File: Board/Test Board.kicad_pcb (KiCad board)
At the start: 2 copper layers, 165.1 x 76.2 mm, 29 parts, among them J1 SCREW TERMINAL, J2 SCREW TERMINAL, J3 SCREW TERMINAL, K1 FINDER-32.21-x300, K2 FINDER-32.21-x300, K3 FINDER-32.21-x300, SW1 UP-MJTP1230, SW2 LT-MJTP1230, SW3 DN-MJTP1230, SW4 RT-MJTP1230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

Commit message: Started re-engineering board
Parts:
- removed K1, K2, K3: FINDER-32.21-x300, Relay_THT:Relay_SPST_Finder_32.21-x300
- added U3: DS1E-M-DC5V, Arduino-Thermostat:DS1E-M-DC5V, F.Cu at (175.0, 34.4)
- added U4: DS1E-M-DC5V, Arduino-Thermostat:DS1E-M-DC5V, F.Cu at (86.2, 86.1)
- added U5: DS1E-M-DC5V, Arduino-Thermostat:DS1E-M-DC5V, F.Cu at (74.1, 86.1)
- C1, C2: value 680uF -> 220uF; footprint Capacitor_THT:CP_Radial_D12.5mm_P5.00mm -> Capacitor_THT:CP_Radial_D10.0mm_P5.00mm
- D2: value SB5199TA -> 31DQ05TA; footprint Diode_THT:D_DO-201_P15.24mm_Horizontal -> Diode_THT:D_DO-201AD_P5.08mm_Vertical_AnodeUp
- L1: footprint Inductor_THT:L_Toroid_Vertical_L21.6mm_W11.4mm_P7.62mm_Pulse_KM-3 -> Inductor_THT:L_Radial_D12.0mm_P5.00mm_Fastron_11P
- R1: value 220R -> XXR; footprint Resistor_THT:R_Axial_DIN0207_L6.3mm_D2.5mm_P7.62mm_Horizontal -> Resistor_SMD:R_1206_3216Metric
- R18, R19, R20, R21, R22: footprint Resistor_THT:R_Axial_DIN0207_L6.3mm_D2.5mm_P7.62mm_Horizontal -> Resistor_SMD:R_1206_3216Metric
- R23: value 220R -> 600R; footprint Resistor_THT:R_Axial_DIN0207_L6.3mm_D2.5mm_P7.62mm_Horizontal -> Resistor_SMD:R_1206_3216Metric
- U6: footprint Sensor:Aosong_DHT11_5.5x12.0_P2.54mm -> Arduino-Thermostat:DHT22-Horizontal
- moved J2 134.5 mm to (175.9, 55.3), turned to 0 degrees
- moved U6 125.0 mm to (75.2, 73.5), turned to 0 degrees
- moved RV1 101.5 mm to (102.4, 87.1), turned to 0 degrees
- moved U1 98.0 mm to (174.8, 69.9)
- moved R23 95.4 mm to (187.4, 40.7), turned to 0 degrees
- moved A1 94.6 mm to (155.1, 37.1), turned to 0 degrees
- moved R22 91.9 mm to (98.6, 99.5)
- moved J3 91.2 mm to (132.4, 88.4), turned to 0 degrees
- moved J1 88.2 mm to (132.4, 76.6), turned to 0 degrees
- moved R19 73.6 mm to (187.3, 34.1), turned to 0 degrees
- moved R18 64.2 mm to (187.3, 37.4)
- moved R21 60.4 mm to (123.6, 72.0)
- moved C1 60.3 mm to (118.8, 96.1), turned to 0 degrees
- moved D2 52.8 mm to (144.4, 85.3), turned to 0 degrees
- moved D1 50.7 mm to (106.9, 73.6), turned to 0 degrees
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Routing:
- net /DHT: track 106.0 -> 0.00 mm
- net Net-(DS1-Pad3): track 74.2 -> 0.00 mm
- net /R: track 67.2 -> 0.00 mm
- net /SW_RT: track 65.1 -> 0.00 mm
- net /COOL: track 63.9 -> 0.00 mm, vias 1 -> 0
- net /SW_UP: track 61.5 -> 0.00 mm
- net Net-(DS1-Pad15): track 60.9 -> 0.00 mm, vias 1 -> 0
- net /D7: track 54.6 -> 0.00 mm
- net /D4: track 54.6 -> 0.00 mm
- net /D6: track 54.6 -> 0.00 mm
- net /D5: track 54.6 -> 0.00 mm
- net /BKLT: track 54.0 -> 0.00 mm
- net +5V: track 52.9 -> 0.00 mm
- net /SW_DN: track 51.0 -> 0.00 mm
- net /E: track 44.1 -> 0.00 mm
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- removed copper zone on B.Cu, net +5V
- removed copper zone on F.Cu, net GND
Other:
- board outline removed
- board text removed: "Designed by A. Elder"

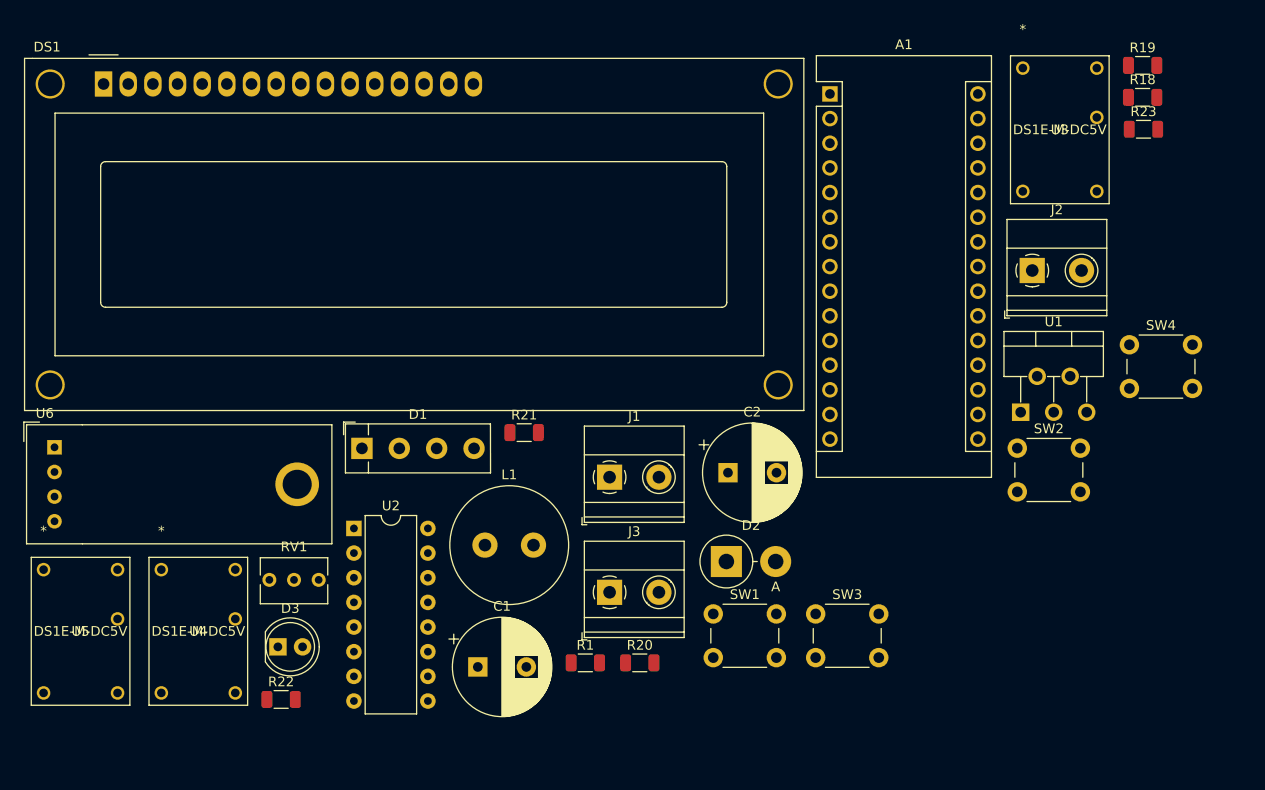
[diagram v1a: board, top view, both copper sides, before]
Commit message: Finish Schematic for new PCB
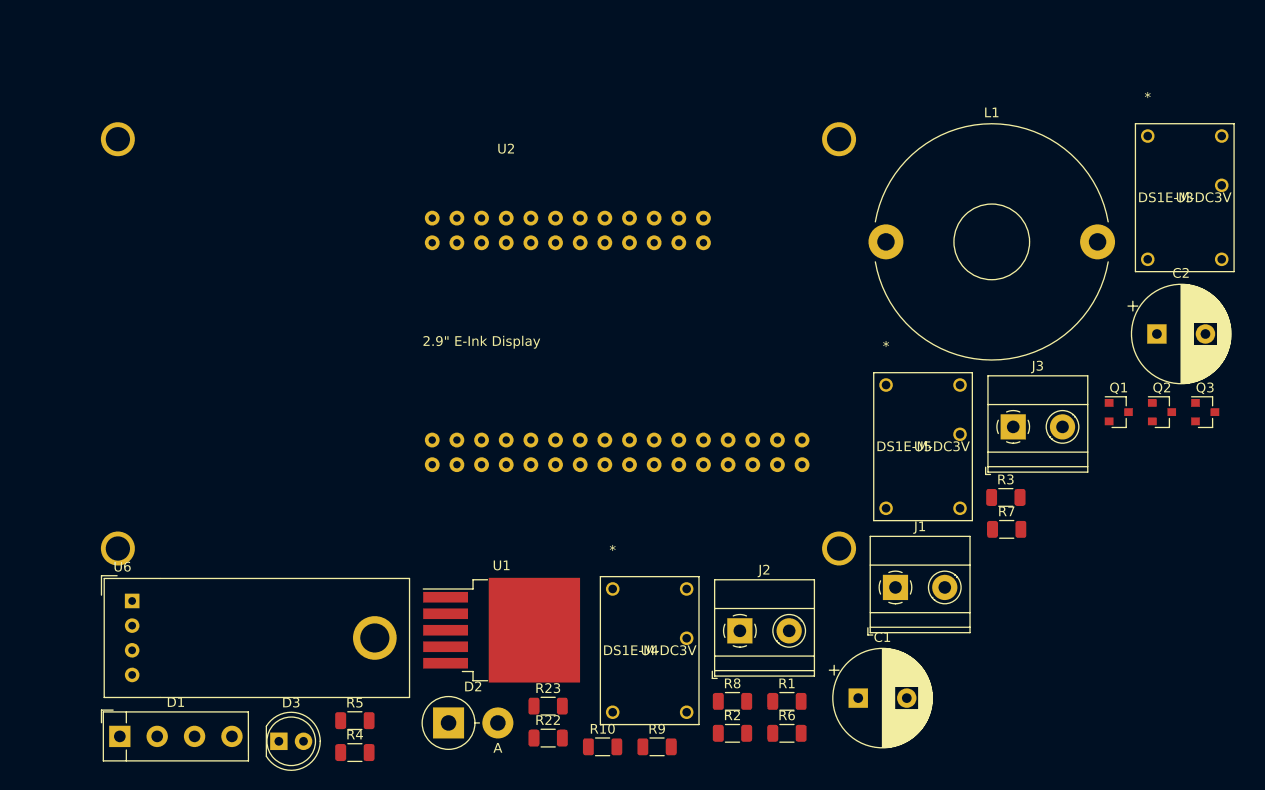
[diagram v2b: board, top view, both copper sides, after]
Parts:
- removed A1: Arduino_Nano_v3.x, Module:Arduino_Nano
- removed DS1: WC1602A, Display:WC1602A
- removed R18, R19, R20, R21: 47k, Resistor_SMD:R_1206_3216Metric
- removed RV1: 10k, Potentiometer_THT:Potentiometer_Bourns_3266Y_Vertical
- removed SW1: UP-MJTP1230, Button_Switch_THT:SW_PUSH_6mm
- removed SW2: LT-MJTP1230, Button_Switch_THT:SW_PUSH_6mm
- removed SW3: DN-MJTP1230, Button_Switch_THT:SW_PUSH_6mm
- removed SW4: RT-MJTP1230, Button_Switch_THT:SW_PUSH_6mm
- added Q1: Q_NMOS_GSD, Package_TO_SOT_SMD:SOT-23, F.Cu at (184.9, 69.9)
- added Q2: Q_NMOS_GSD, Package_TO_SOT_SMD:SOT-23, F.Cu at (189.3, 69.9)
- added Q3: Q_NMOS_GSD, Package_TO_SOT_SMD:SOT-23, F.Cu at (193.8, 69.9)
- added R10: 1.5K, Resistor_SMD:R_1206_3216Metric, F.Cu at (131.7, 104.3)
- added R2: 10K, Resistor_SMD:R_1206_3216Metric, F.Cu at (145.1, 103.0)
- added R3: 10K, Resistor_SMD:R_1206_3216Metric, F.Cu at (173.2, 78.7)
- added R4: 1K, Resistor_SMD:R_1206_3216Metric, F.Cu at (106.2, 104.9)
- added R5: 1K, Resistor_SMD:R_1206_3216Metric, F.Cu at (106.2, 101.6)
- added R6: 1K, Resistor_SMD:R_1206_3216Metric, F.Cu at (150.7, 103.0)
- added R7: 4.7K, Resistor_SMD:R_1206_3216Metric, F.Cu at (173.3, 81.9)
- added R8: 2.0k, Resistor_SMD:R_1206_3216Metric, F.Cu at (145.1, 99.7)
- added R9: 820R, Resistor_SMD:R_1206_3216Metric, F.Cu at (137.3, 104.3)
- L1: value 53uH -> 68uH; footprint Inductor_THT:L_Radial_D12.0mm_P5.00mm_Fastron_11P -> Inductor_THT:L_Toroid_Horizontal_D24.1mm_P21.80mm_Bourns_2200
- R1: value XXR -> 10K
- U1: value LM2596T-5 -> LM2596S-3.3; footprint Package_TO_SOT_THT:TO-220-5_P3.4x3.7mm_StaggerOdd_Lead3.8mm_Vertical -> Package_TO_SOT_SMD:TO-263-5_TabPin3
- U2: value L293D -> Adafruit-Eink-Display; footprint Package_DIP:DIP-16_W7.62mm -> Arduino-Thermostat:Adafruit-eink-display
- U3, U4, U5: value DS1E-M-DC5V -> DS1E-M-DC3V
- moved U5 88.8 mm to (160.9, 67.1)
- moved R23 85.4 mm to (126.1, 100.2)
- moved U1 58.0 mm to (121.3, 92.3)
- moved L1 51.8 mm to (160.9, 52.3)
- moved J2 47.8 mm to (145.8, 92.4)
- moved U4 46.5 mm to (132.7, 88.1)
- moved C2 46.4 mm to (188.8, 61.8)
- moved J3 44.9 mm to (174.0, 71.4)
- moved U2 42.6 mm to (121.8, 42.3)
- moved C1 39.3 mm to (158.0, 99.3)
- moved D1 38.8 mm to (82.0, 103.3)
- moved D2 33.1 mm to (115.8, 101.9)
- moved J1 31.6 mm to (161.9, 87.9)
- moved R22 27.8 mm to (126.1, 103.4)
- moved R1 21.1 mm to (150.7, 99.7)
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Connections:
- C2 pad 1: +5V -> +3V3
- D3 pad 2: +5V -> +3V3
- L1 pad 2: +5V -> +3V3
- R1 pad 2: /BACKLIGHT -> GND
- R22 pad 2: +5V -> +3V3
- U1 pad 4: +5V -> +3V3
- U2 pad 1: +5V -> /RESET
- U2 pad 10: /COOL -> Net-(U2-Pad10)
- U2 pad 11: /COOLRLY -> SCK
- U2 pad 12: GND -> MOSI
- U2 pad 13: GND -> MISO
- U2 pad 14: /BACKLIGHT -> Net-(U2-Pad14)
- U2 pad 15: /BKLT -> Net-(U2-Pad15)
- U2 pad 16: +5V -> Net-(U2-Pad16)
- U2 pad 2: /FAN -> +3V3
- U2 pad 3: /FANRLY -> Net-(U2-Pad3)
- U2 pad 5: GND -> Net-(U2-Pad5)
- U2 pad 6: /HEATRLY -> Net-(U2-Pad6)
- U2 pad 7: /HEAT -> Net-(U2-Pad7)
- U2 pad 8: +5V -> Net-(U2-Pad8)
- U2 pad 9: +5V -> Net-(U2-Pad9)
- U3 pad 1: GND -> /FANRLY
- U3 pad 6: /FANRLY -> +3V3
- U4 pad 1: GND -> /HEATRLY
- U4 pad 6: /HEATRLY -> +3V3
- U5 pad 1: GND -> /COOLRLY
- U5 pad 6: /COOLRLY -> +3V3
- U6 pad 1: +5V -> +3V3

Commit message: Continue V2 Design
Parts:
- added A1: Adafruit_Feather_HUZZAH_ESP8266, Module:Adafruit_Feather, F.Cu at (237.0, 51.0)
- C1, C2: value 220uF -> 680uF; footprint Capacitor_THT:CP_Radial_D10.0mm_P5.00mm -> Capacitor_THT:CP_Radial_D18.0mm_P7.50mm
- D1: footprint Diode_THT:Diode_Bridge_Vishay_KBPM -> Arduino-Thermostat:Diode Bridge 4-SMD
- D2: value 31DQ05TA -> VS-50WQ04FNTR-M3; footprint Diode_THT:D_DO-201AD_P5.08mm_Vertical_AnodeUp -> Package_TO_SOT_SMD:TO-252-3_TabPin2
- L1: footprint Inductor_THT:L_Toroid_Horizontal_D24.1mm_P21.80mm_Bourns_2200 -> Inductor_THT:L_Radial_L16.1mm_W16.1mm_Px7.62mm_Py12.70mm_Pulse_LP-44
- moved U2 55.9 mm to (68.5, 25.5)
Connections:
- J3 pad 2: Net-(J3-Pad2) -> unconnected-(J3-Pad2)
- U2 pad 10: Net-(U2-Pad10) -> unconnected-(U2-Pad10)
- U2 pad 14: Net-(U2-Pad14) -> unconnected-(U2-Pad14)
- U2 pad 15: Net-(U2-Pad15) -> unconnected-(U2-Pad15)
- U2 pad 16: Net-(U2-Pad16) -> unconnected-(U2-Pad16)
- U2 pad 17: Net-(U2-Pad17) -> unconnected-(U2-Pad17)
- U2 pad 18: Net-(U2-Pad18) -> unconnected-(U2-Pad18)
- U2 pad 19: Net-(U2-Pad19) -> unconnected-(U2-Pad19)
- U2 pad 20: Net-(U2-Pad20) -> unconnected-(U2-Pad20)
- U2 pad 26: Net-(U2-Pad26) -> unconnected-(U2-Pad26)
- U2 pad 27: Net-(U2-Pad27) -> unconnected-(U2-Pad27)
- U2 pad 28: Net-(U2-Pad28) -> unconnected-(U2-Pad28)
- U2 pad 3: Net-(U2-Pad3) -> unconnected-(U2-Pad3)
- U2 pad 5: Net-(U2-Pad5) -> unconnected-(U2-Pad5)
- U2 pad 6: Net-(U2-Pad6) -> unconnected-(U2-Pad6)
- U2 pad 7: Net-(U2-Pad7) -> unconnected-(U2-Pad7)
- U2 pad 8: Net-(U2-Pad8) -> unconnected-(U2-Pad8)
- U2 pad 9: Net-(U2-Pad9) -> unconnected-(U2-Pad9)
- U3 pad 10: Net-(U3-Pad10) -> unconnected-(U3-Pad10)
- U4 pad 10: Net-(U4-Pad10) -> unconnected-(U4-Pad10)
- U5 pad 10: Net-(U5-Pad10) -> unconnected-(U5-Pad10)
- U6 pad 3: Net-(U6-Pad3) -> unconnected-(U6-Pad3)
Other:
- net class Default removed

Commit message: Continue board layout for v2 design
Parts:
- added D4: D, Diode_SMD:D_SMA_Handsoldering, F.Cu at (140.0, 99.9)
- added D5: D, Diode_SMD:D_SMA_Handsoldering, F.Cu at (140.0, 133.9)
- added D6: D, Diode_SMD:D_SMA_Handsoldering, F.Cu at (140.0, 116.9)
- added R11: 470R, Resistor_SMD:R_1206_3216Metric, F.Cu at (185.0, 112.0)
- added SW1: SW_Push, Button_Switch_THT:SW_PUSH_6mm_H5mm, F.Cu at (177.8, 122.8)
- added SW2: SW_Push, Button_Switch_THT:SW_PUSH_6mm_H5mm, F.Cu at (177.8, 132.8)
- added SW3: SW_Push, Button_Switch_THT:SW_PUSH_6mm_H5mm, F.Cu at (166.8, 127.8)
- added SW4: SW_Push, Button_Switch_THT:SW_PUSH_6mm_H5mm, F.Cu at (188.8, 127.8)
- D3: footprint LED_THT:LED_D5.0mm -> LED_SMD:LED_1206_3216Metric_Pad1.42x1.75mm_HandSolder
- R8: value 2.0k -> 2.0K
- R9: value 820R -> 4.3K
- moved U2 156.1 mm to (221.9, 54.4)
- moved U6 147.6 mm to (230.0, 105.0)
- moved R22 95.0 mm to (221.0, 106.0), turned to 90 degrees
- moved U3 83.4 mm to (135.5, 106.3), turned to 180 degrees
- moved J3 82.3 mm to (113.7, 127.5), turned to -90 degrees
- moved Q3 80.0 mm to (146.0, 134.0), turned to 180 degrees
- moved D3 72.8 mm to (170.0, 90.9), turned to 90 degrees
- moved A1 69.8 mm to (253.1, 118.9), turned to -90 degrees
- moved U5 61.7 mm to (135.5, 123.3), turned to 180 degrees
- moved Q1 61.1 mm to (146.0, 117.0), turned to 180 degrees
- moved R3 59.6 mm to (151.0, 134.0), turned to 90 degrees
- moved C1 58.0 mm to (119.5, 56.0), turned to 180 degrees
- moved Q2 52.8 mm to (146.0, 100.0), turned to 180 degrees
- moved U4 52.3 mm to (135.5, 140.3), turned to 180 degrees
- moved R4 52.2 mm to (156.5, 119.0)
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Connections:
- A1 pad 18: /DHT -> /FAN
- A1 pad 19: /FAN -> /DHT
- R10 pad 1: /BUTTON3 -> Net-(R10-Pad1)
- R10 pad 2: /BUTTON2 -> /ADC
- R9 pad 1: /BUTTON2 -> Net-(R9-Pad1)
- U2 pad 23: /ADC -> unconnected-(U2-Pad23)
- U2 pad 24: /BUTTON2 -> unconnected-(U2-Pad24)
- U2 pad 25: /BUTTON3 -> unconnected-(U2-Pad25)
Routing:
- net /C: track 0.00 -> 26.5 mm
- net /R: track 0.00 -> 20.4 mm
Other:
- board outline added: 160 x 100 mm

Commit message: Finished board layout, updated readme
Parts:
- added F1: Fuse, Fuse:Fuseholder_Blade_Mini_Keystone_3568, F.Cu at (72.6, 91.0)
- added G***: LOGO, LOGO, F.Cu at (119.0, 86.5)
- moved C2 42.5 mm to (124.0, 56.5), turned to 90 degrees
- moved C1 41.0 mm to (78.5, 57.0), turned to 90 degrees
- moved D1 38.6 mm to (77.0, 71.0)
- moved L1 38.0 mm to (97.2, 75.8)
- moved U1 37.8 mm to (101.2, 52.0), turned to 90 degrees
- moved U3 37.6 mm to (98.0, 103.3)
- moved U4 37.6 mm to (98.0, 137.3)
- moved U5 37.6 mm to (98.0, 120.3)
- moved A1 37.6 mm to (215.6, 115.9)
- moved D2 37.6 mm to (115.0, 68.8)
- moved D3 37.6 mm to (132.5, 87.9)
- moved D4 37.6 mm to (102.5, 96.9)
- moved D5 37.6 mm to (102.5, 130.9)
- moved D6 37.6 mm to (102.5, 113.9)
- moved J1 37.6 mm to (76.2, 98.4)
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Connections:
- J1 pad 1: /R -> Net-(J1-Pad1)
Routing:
- net /DC: track 0.00 -> 136.1 mm
- net /ECS: track 0.00 -> 136.0 mm
- net /ADC: track 0.00 -> 100.8 mm, vias 0 -> 1
- net /FAN: track 0.00 -> 89.9 mm, vias 0 -> 1
- net /COOL: track 0.00 -> 71.3 mm
- net /HEAT: track 0.00 -> 69.1 mm
- net +3V3: track 0.00 -> 63.7 mm, vias 0 -> 2
- net /DHT: track 0.00 -> 53.7 mm, vias 0 -> 1
- net MISO: track 0.00 -> 37.9 mm
- net /RESET: track 0.00 -> 36.3 mm
- net +VDC: track 0.00 -> 35.6 mm
- net SCK: track 0.00 -> 34.3 mm
- net MOSI: track 0.00 -> 34.3 mm
- net Net-(R9-Pad1): track 0.00 -> 27.9 mm
- net /G: track 0.00 -> 26.7 mm
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- added copper zone on B.Cu, net +3V3
- added copper zone on B.Cu, net /R
- added copper zone on F.Cu, net GND
- added copper zone on F.Cu, net Net-(D2-Pad1)
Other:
- outline, holes or cut-outs redrawn
- board text added: "C"
- board text added: "Designed by A. Elder freeport7.space"
- board text added: "G"
- board text added: "NC"
- board text added: "R"
- board text added: "W"
- board text added: "Y"
